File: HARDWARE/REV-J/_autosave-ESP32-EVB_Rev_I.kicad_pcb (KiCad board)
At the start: 2 copper layers, 75.2 x 74.7 mm, 157 parts, among them CON1 TB3 DG306-5.0-3P, CON2 TB3 DG306-5.0-3P, Q1 BC817-40(SOT23), Q2 BC817-40(SOT23), Q3 Q12MHz/20pF/30ppm/2P/HC-49SM(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, Q4 BC817-40(SOT23), Q5 BC817-40(SOT23), Q6 BC817, Q7 BC817-40(SOT23), U1 BL4054B-42TPRN(SOT23-5), U10 BAT54C(SOT23-3), U2 SY8089AAAC(SOT23-5), U3 ESP-WROOM-32, U4 LAN8710A-EZC(QFN32), U5 CH340T(SSOP20W), U6 MCP2562-E/SN(SOIC-8_150mil), U7 RPM7236-H8, U8 NCP303LSN27T1G(SOT-23-5), U9 BAT54C(SOT23-3)

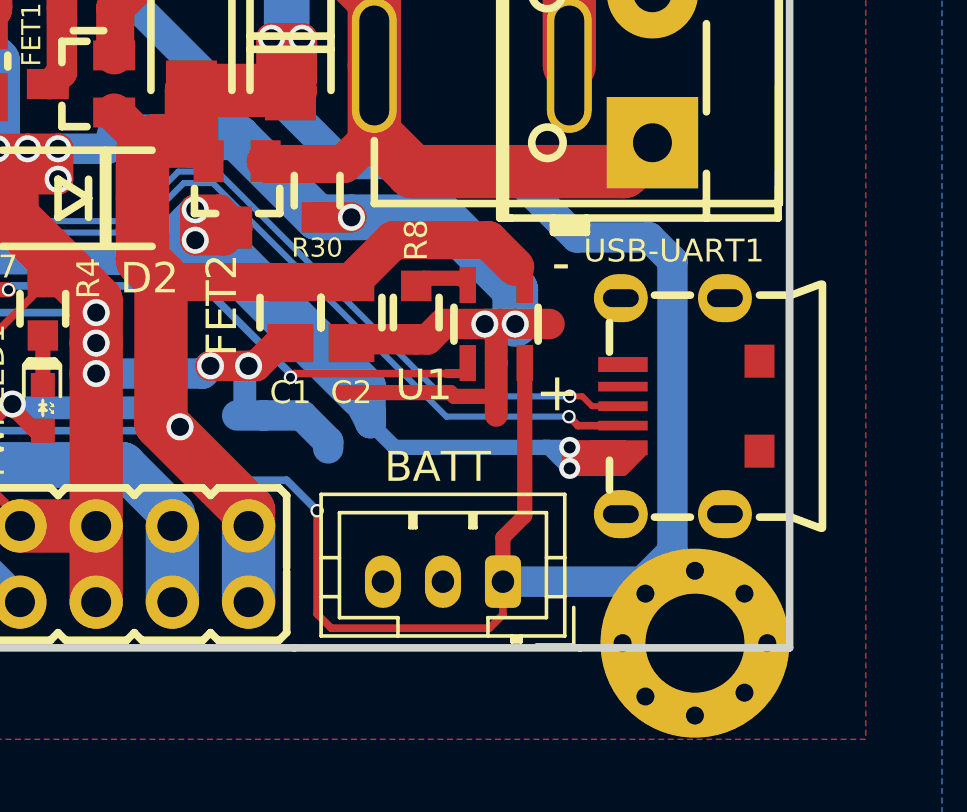
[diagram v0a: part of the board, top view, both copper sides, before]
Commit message: re-position usb port+bat conector
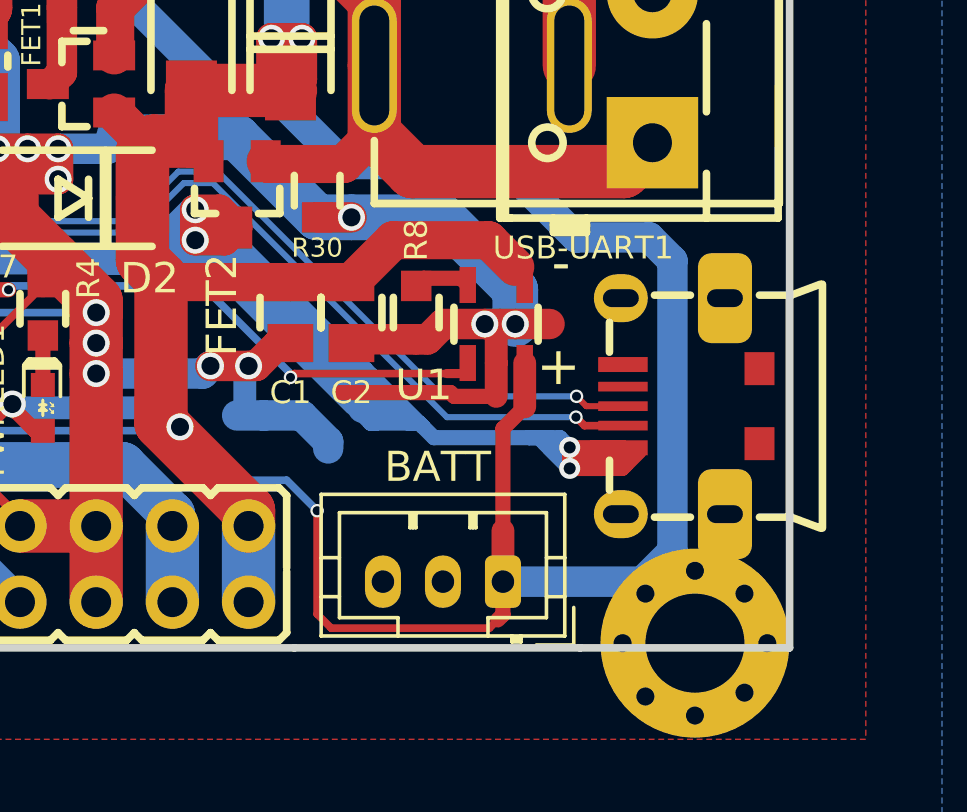
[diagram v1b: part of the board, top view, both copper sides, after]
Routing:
- net /+5V_USB: track 101.8 -> 111.0 mm
- net GND: track 1011.1 -> 1010.4 mm

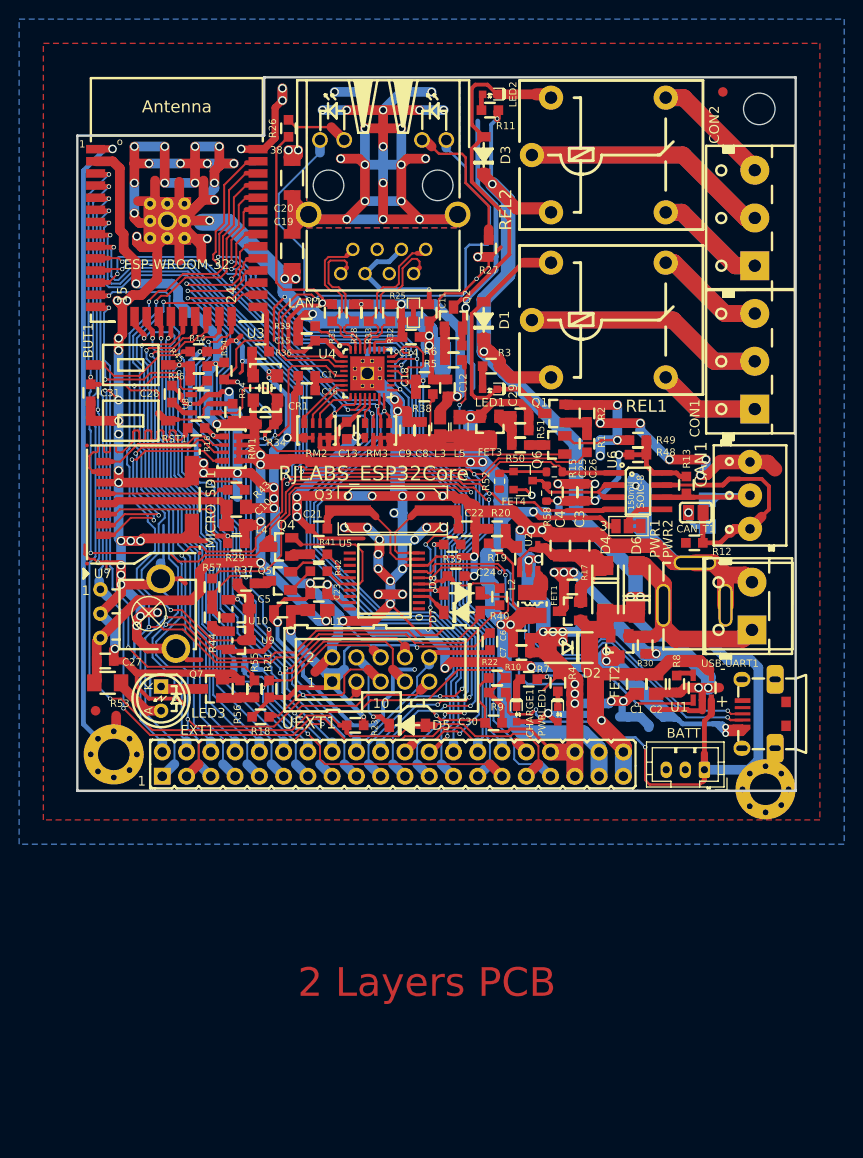
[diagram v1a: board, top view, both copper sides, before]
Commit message: done add 5 extension UEXT
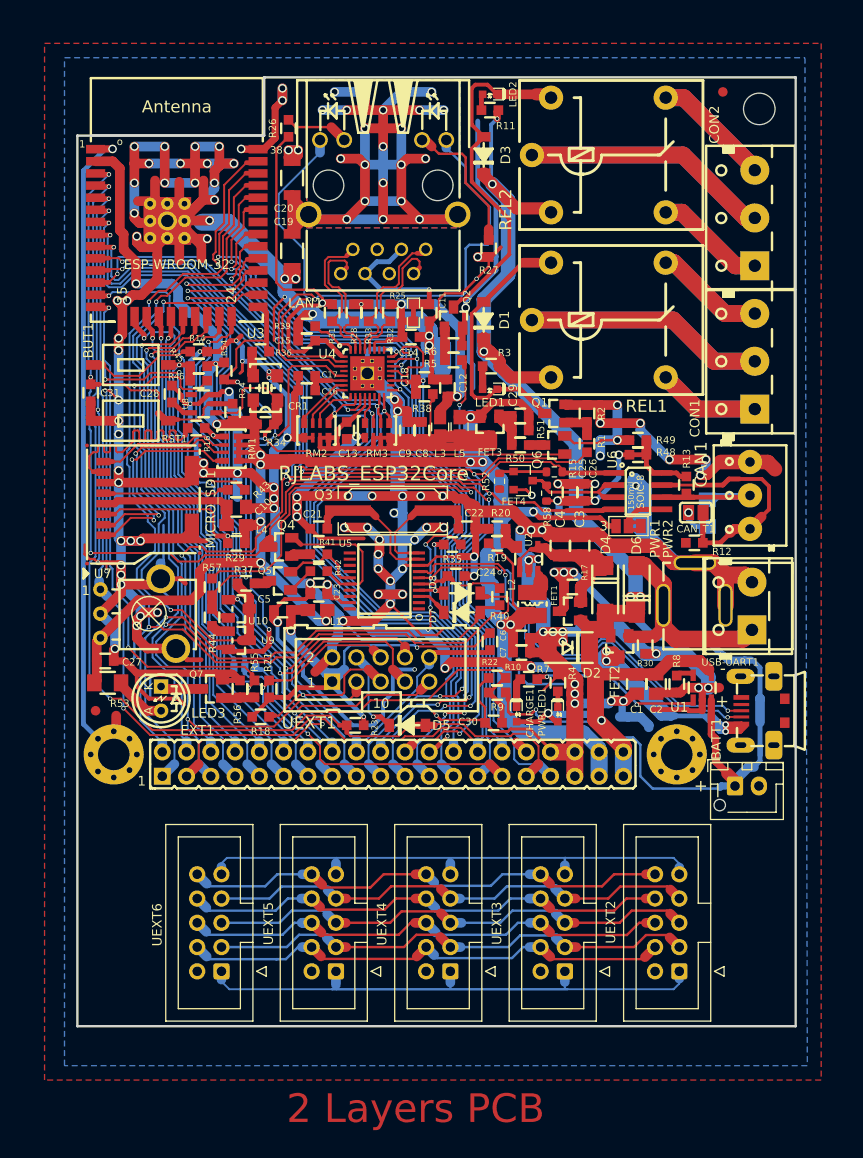
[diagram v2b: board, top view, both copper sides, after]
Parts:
- removed BATT: Conn_01x03, Connector_JST:JST_PH_B3B-PH-K_1x03_P2.00mm_Vertical
- added BATT1: Conn_01x02, Connector_JST:JST_XH_B2B-XH-AM_1x02_P2.50mm_Vertical, F.Cu at (138.4, 141.2)
- added UEXT2: BH10S, Connector_IDC:IDC-Header_2x05_P2.54mm_Vertical, F.Cu at (132.6, 160.6)
- added UEXT3: BH10S, Connector_IDC:IDC-Header_2x05_P2.54mm_Vertical, F.Cu at (120.6, 160.6)
- added UEXT4: BH10S, Connector_IDC:IDC-Header_2x05_P2.54mm_Vertical, F.Cu at (108.6, 160.6)
- added UEXT5: BH10S, Connector_IDC:IDC-Header_2x05_P2.54mm_Vertical, F.Cu at (96.7, 160.6)
- added UEXT6: BH10S, Connector_IDC:IDC-Header_2x05_P2.54mm_Vertical, F.Cu at (84.7, 160.6)
- moved MH2 9.98 mm to (132.3, 137.9)
- moved USB-UART1 0.35 mm to (142.2, 133.3)
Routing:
- net Net-(UEXT2-Pad1): track 0.00 -> 57.8 mm
- net Net-(UEXT2-Pad9): track 0.00 -> 55.9 mm
- net Net-(UEXT2-Pad6): track 0.00 -> 53.1 mm
- net Net-(UEXT2-Pad4): track 0.00 -> 52.4 mm
- net Net-(UEXT2-Pad7): track 0.00 -> 52.3 mm
- net Net-(UEXT2-Pad10): track 0.00 -> 52.2 mm
- net Net-(UEXT2-Pad3): track 0.00 -> 52.1 mm
- net Net-(UEXT2-Pad5): track 0.00 -> 52.1 mm
- net Net-(UEXT2-Pad8): track 0.00 -> 52.0 mm
- net Net-(BATT1-Pad1): track 88.8 -> 97.4 mm, vias 5 -> 4
- net /+5V_USB: track 111.0 -> 111.8 mm
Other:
- board size 75.2 x 74.7 mm -> 75.2 x 99.3 mm
